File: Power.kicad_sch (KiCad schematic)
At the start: 11 parts, among them J1 BAT, J3 USB_C_Receptacle, U4 LM5156HPWPR, U5 MCP73831T-2ACI/OT

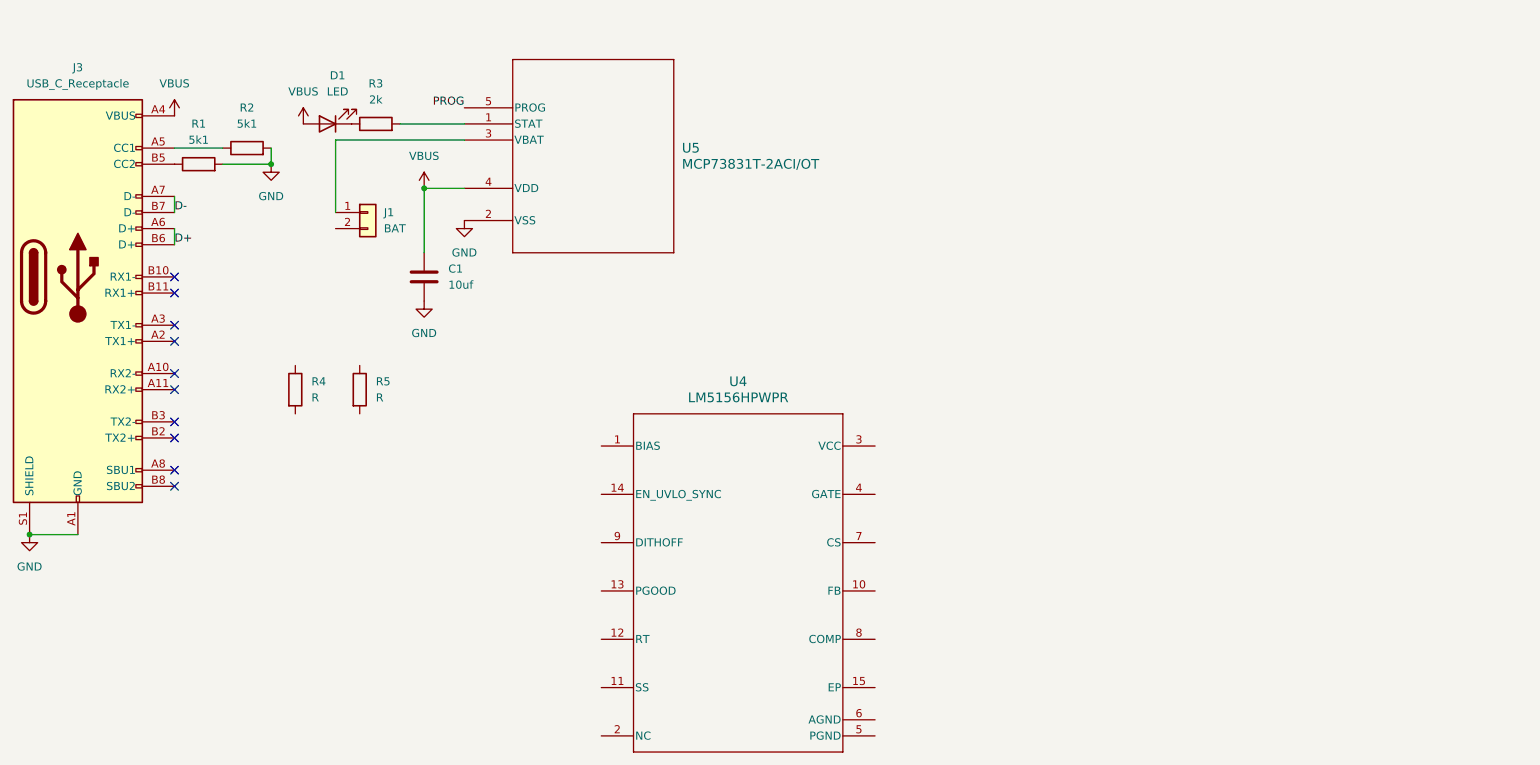
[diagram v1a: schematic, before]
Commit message: Additional sheets in the schematic
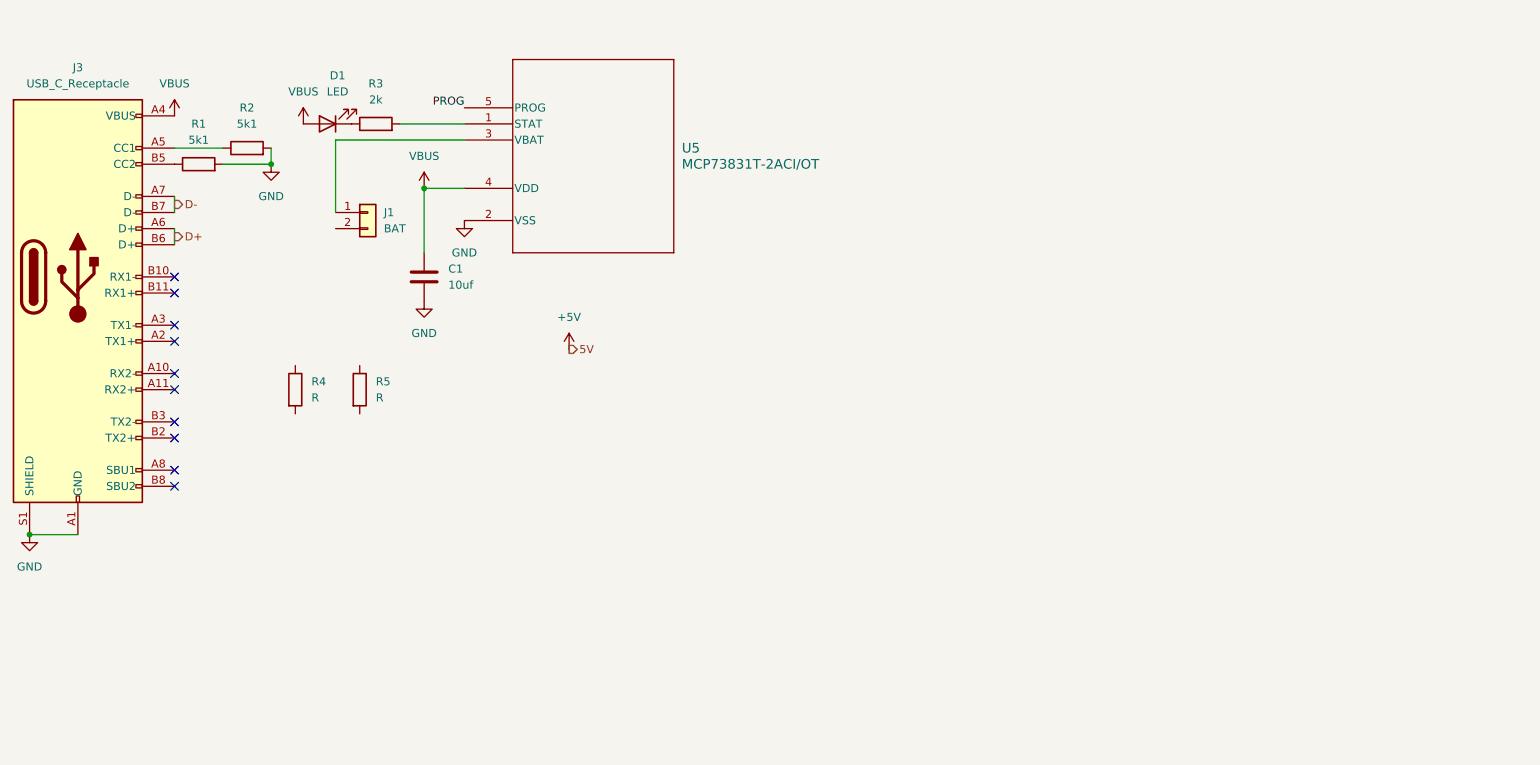
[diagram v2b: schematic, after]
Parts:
- removed U4: LM5156HPWPR, PWP0014H-IPC_A, symbol LM5156H:LM5156HPWPR
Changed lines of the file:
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@@
     (stroke (width 0) (type default))
-  )
-  (label "D-" (at 45.72 43.18 0) (fields_autoplaced)
-    (effects (font (size 1.27 1.27)) (justify left bottom))
   )
   (label "PROG" (at 91.44 26.67 180) (fields_autoplaced)
     (effects (font (size 1.27 1.27)) (justify right bottom))
   )
-  (label "D+" (at 45.72 48.26 0) (fields_autoplaced)
-    (effects (font (size 1.27 1.27)) (justify left bottom))
+  (hierarchical_label "D+" (shape output) (at 45.72 46.99 0) (fields_autoplaced)
+    (effects (font (size 1.27 1.27)) (justify left))
   )
-  (symbol (lib_id "LM5156H:LM5156HPWPR") (at 113.03 80.01 0) (unit 1)
-    (in_bom yes) (on_board yes) (dnp no) (fields_autoplaced)
-    (property "Reference" "U4" (at 134.62 69.85 0)
-      (effects (font (size 1.524 1.524)))
-    )
-    (property "Value" "LM5156HPWPR" (at 134.62 72.39 0)
-      (effects (font (size 1.524 1.524)))
-    )
-    (property "Footprint" "PWP0014H-IPC_A" (at 113.03 80.01 0)
-      (effects (font (size 1.27 1.27) italic) hide)
-    )
-    (property "Datasheet" "LM5156HPWPR" (at 113.03 80.01 0)
-      (effects (font (size 1.27 1.27) italic) hide)
-    )
-    (pin "1")
-    (pin "10")
-    (pin "11")
-    (pin "12")
-    (pin "13")
-    (pin "14")
-    (pin "15")
-    (pin "2")
-    (pin "3")
-    (pin "4")
-    (pin "5")
-    (pin "6")
-    (pin "7")
-    (pin "8")
-    (pin "9")
-    (instances
-      (project "Pico-Skidi"
-        (path "/21865b85-eb74-4d61-a31a-30858d3bc341"
-          (reference "U4") (unit 1)
-        )
-        (path "/21865b85-eb74-4d61-a31a-30858d3bc341/8900a908-b882-43c5-abd2-34b7e0cc181b"
-          (reference "U4") (unit 1)
-        )
-      )
-    )
+  (hierarchical_label "D-" (shape output) (at 45.72 41.91 0) (fields_autoplaced)
+    (effects (font (size 1.27 1.27)) (justify left))
+  )
+  (hierarchical_label "5V" (shape output) (at 107.95 64.77 0) (fields_autoplaced)
+    (effects (font (size 1.27 1.27)) (justify left))
   )
   (symbol (lib_id "power:VBUS") (at 45.72 27.94 0) (unit 1)
@@
         )
       )
+    )
+  )
+  (symbol (lib_id "power:+5V") (at 107.95 64.77 0) (unit 1)
+    (in_bom yes) (on_board yes) (dnp no) (fields_autoplaced)
+    (property "Reference" "#PWR010" (at 107.95 68.58 0)
+      (effects (font (size 1.27 1.27)) hide)
+    )
+    (property "Value" "+5V" (at 107.95 59.69 0)
+      (effects (font (size 1.27 1.27)))
+    )
+    (property "Footprint" "" (at 107.95 64.77 0)
+      (effects (font (size 1.27 1.27)) hide)
+    )
+    (property "Datasheet" "" (at 107.95 64.77 0)
+      (effects (font (size 1.27 1.27)) hide)
+    )
+    (pin "1")
+    (instances
+      (project "Pico-Skidi"
+        (path "/21865b85-eb74-4d61-a31a-30858d3bc341/8900a908-b882-43c5-abd2-34b7e0cc181b"
+          (reference "#PWR010") (unit 1)
+        )
+      )

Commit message: Lots of changes
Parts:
- added Q1: Q_PMOS_GDS, symbol Device:Q_PMOS_GDS
- C1: footprint (none) -> Capacitor_SMD:C_0603_1608Metric_Pad1.08x0.95mm_HandSolder
- D1: footprint (none) -> LED_SMD:LED_0603_1608Metric_Pad1.05x0.95mm_HandSolder
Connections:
- net +5V: now also Q1.3 (S)
- net VBUS: now also Q1.1 (G)
- new net Batt_Source: Q1.2 (D)

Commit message: syncing
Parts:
- removed R4: R, symbol Device:R
- added C2: 0.1uF, Capacitor_SMD:C_0603_1608Metric_Pad1.08x0.95mm_HandSolder, symbol Device:C
- added C3: C, Capacitor_SMD:C_0603_1608Metric_Pad1.08x0.95mm_HandSolder, symbol Device:C
- added D1: LED, LED_SMD:LED_0603_1608Metric_Pad1.05x0.95mm_HandSolder, symbol Device:LED
- added Q2, Q3: Q_NMOS_DGS, Connector_PinHeader_2.54mm:PinHeader_1x03_P2.54mm_Vertical, symbol Device:Q_NMOS_DGS
- added R3: 2k, Resistor_SMD:R_0603_1608Metric_Pad0.98x0.95mm_HandSolder, symbol Device:R
- added R6: 3k3, Resistor_SMD:R_0603_1608Metric_Pad0.98x0.95mm_HandSolder, symbol Device:R
- added R7: 330, Resistor_SMD:R_0603_1608Metric_Pad0.98x0.95mm_HandSolder, symbol Device:R
- added R8: 2.2k, Resistor_SMD:R_0603_1608Metric_Pad0.98x0.95mm_HandSolder, symbol Device:R
- added U2: BQ29700DSER, BQ29700DSER:DSE0006A, symbol BQ29700DSER:BQ29700DSER
- J1: footprint (none) -> Connector_JST:JST_PH_S2B-PH-K_1x02_P2.00mm_Horizontal
- J3: footprint (none) -> Connector_USB:USB_C_Plug_Molex_105444
- Q1: footprint (none) -> Connector_PinHeader_2.54mm:PinHeader_1x03_P2.54mm_Vertical
- R1, R2, R3: footprint (none) -> Resistor_SMD:R_0603_1608Metric_Pad0.98x0.95mm_HandSolder
- R5: value R -> 4k99; footprint (none) -> Resistor_SMD:R_0603_1608Metric_Pad0.98x0.95mm_HandSolder
- U5: footprint SOT-23-5_MC_MCH -> MCP73831:SOT-23-5_MC_MCH
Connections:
- net PROG is gone; now on an unnamed net: U5.5 (PROG)
- net GND: now also J1.1 (Pin_1), R5.1, U5.3 (VBAT), C2.2, C3.1, C3.2, D1.1 (K), Q3.3 (S), R6.2, R7.1, U2.4 (VSS)
- net BAT_GND: now reaches J1.2 (Pin_2)
- net at R5.2: now also R6.1
- new net: Q2.2 (G), U2.2 (COUT)
- new net: Q3.2 (G), U2.3 (DOUT)
- new net: C2.1, R7.2, U2.5 (BAT)
- new net: R8.1, U2.6 (V-)
- new net: Q2.1 (D), Q3.1 (D)
- new net: Q2.3 (S), R8.2
- new net POWER_LED_A: D1.2 (A), R3.2
- new net VSYS: R3.1
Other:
- note added: "Adding both resistors here sets current limit to ~500mA"
- moved on the sheet: C1, D1, J1, Q1, R3, U5
